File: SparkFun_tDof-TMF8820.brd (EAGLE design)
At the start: 25.4 x 25.4 mm, 29 parts, among them J4 QWIIC_RIGHT_ANGLE, J5 QWIIC_RIGHT_ANGLE

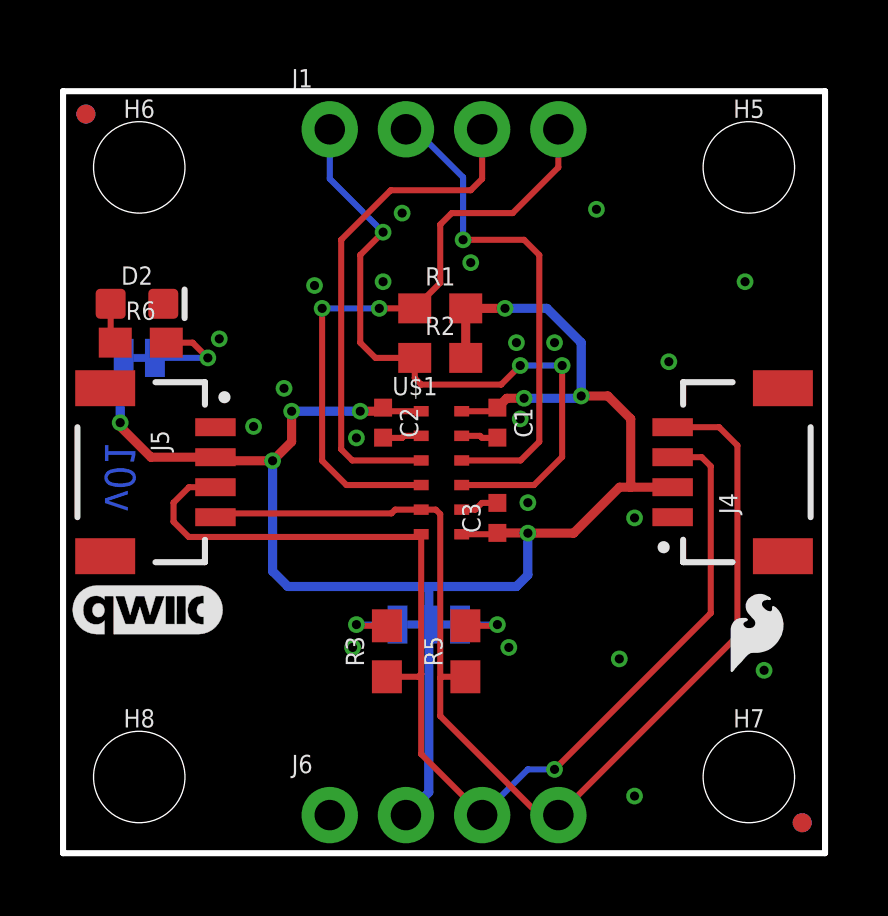
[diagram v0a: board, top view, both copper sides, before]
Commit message: Adds silk to TMF8820, updates footprint with pin 1 indicator
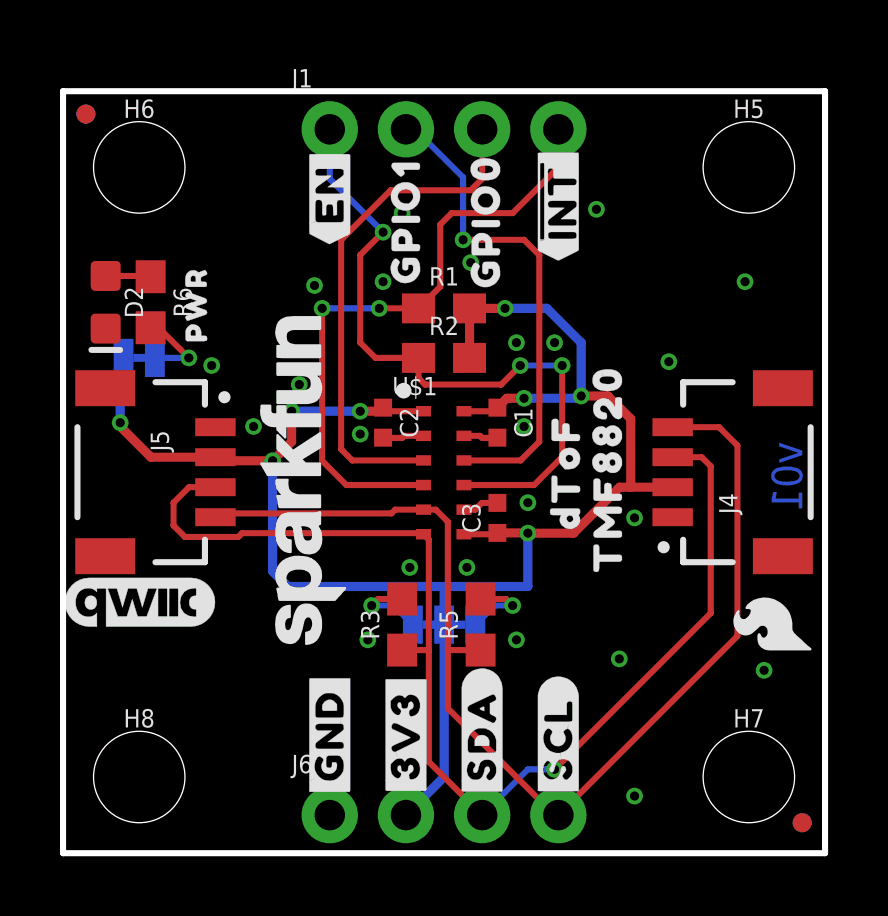
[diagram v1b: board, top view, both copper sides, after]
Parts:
- added U$10: (no value), TMFTopSilk:##INT##8
- added U$11: (no value), TMFTopSilk:TMF88209
- added U$12: (no value), TMFTopSilk:DTOF882188211
- added U$13: (no value), SparkFun-Aesthetics:SFE_LOGO_NAME_.1
- added U$14: (no value), TMFTopSilk:PWR882188212
- added U$15: (no value), TMFBotSilk:##INT##9
- added U$16: (no value), TMFBotSilk:#3V3#0
- added U$17: (no value), TMFBotSilk:#EN#7
- added U$18: (no value), TMFBotSilk:#GND#4
- added U$19: (no value), TMFBotSilk:#GPIO1#8
- added U$2: (no value), TMFTopSilk:#3V3#0
- added U$20: (no value), TMFBotSilk:#I2C#11
- added U$21: (no value), TMFBotSilk:#SCL#5
- added U$22: (no value), TMFBotSilk:#LED#10
- added U$23: (no value), TMFBotSilk:#SDA#6
- added U$24: (no value), TMFBotSilk:#SYNC#8
- added U$26: (no value), TMFTopSilk:TMF882021
- added U$27: (no value), TMFTopSilk:DTOF8821882023
- added U$28: (no value), TMFBotSilk:DEF11
- added U$29: (no value), TMFBotSilk:ADDR#12
- added U$3: (no value), TMFTopSilk:#GND#4
- added U$30: (no value), TMFBotSilk:0X4113
- added U$4: (no value), TMFTopSilk:#SDA#6
- added U$5: (no value), TMFTopSilk:#SCL#5
- added U$7: (no value), TMFTopSilk:#EN#7
- added U$8: (no value), TMFTopSilk:GPIO18
- added U$9: (no value), TMFTopSilk:GPIO019
- moved LOGO4 16.2 mm to (35.3, 32.6)
- moved LOGO3 6.22 mm to (45.7, 40.8)
- moved R6 1.39 mm to (35.9, 45.0), turned to 270 degrees
- moved D2 1.04 mm to (34.4, 45.0), turned to 270 degrees
- moved R3 1.02 mm to (44.3, 34.3)
- moved R5 1.02 mm to (46.9, 34.3)
- moved U$25 0.57 mm to (56.6, 34.3), turned to 90 degrees
- moved I2C 0.51 mm to (45.7, 34.3)
- moved U$6 0.36 mm to (35.6, 35.1)
- moved R1 0.13 mm to (45.7, 44.8)
- moved R2 0.13 mm to (45.7, 43.2)
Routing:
- net N$6: track 3.36 -> 2.82 mm
- net GND: track 3.81 -> 3.73 mm, vias 21 -> 23
